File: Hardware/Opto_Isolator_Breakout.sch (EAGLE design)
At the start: 16 parts, among them Q1 NPN, Q2 NPN, U1 OPTO

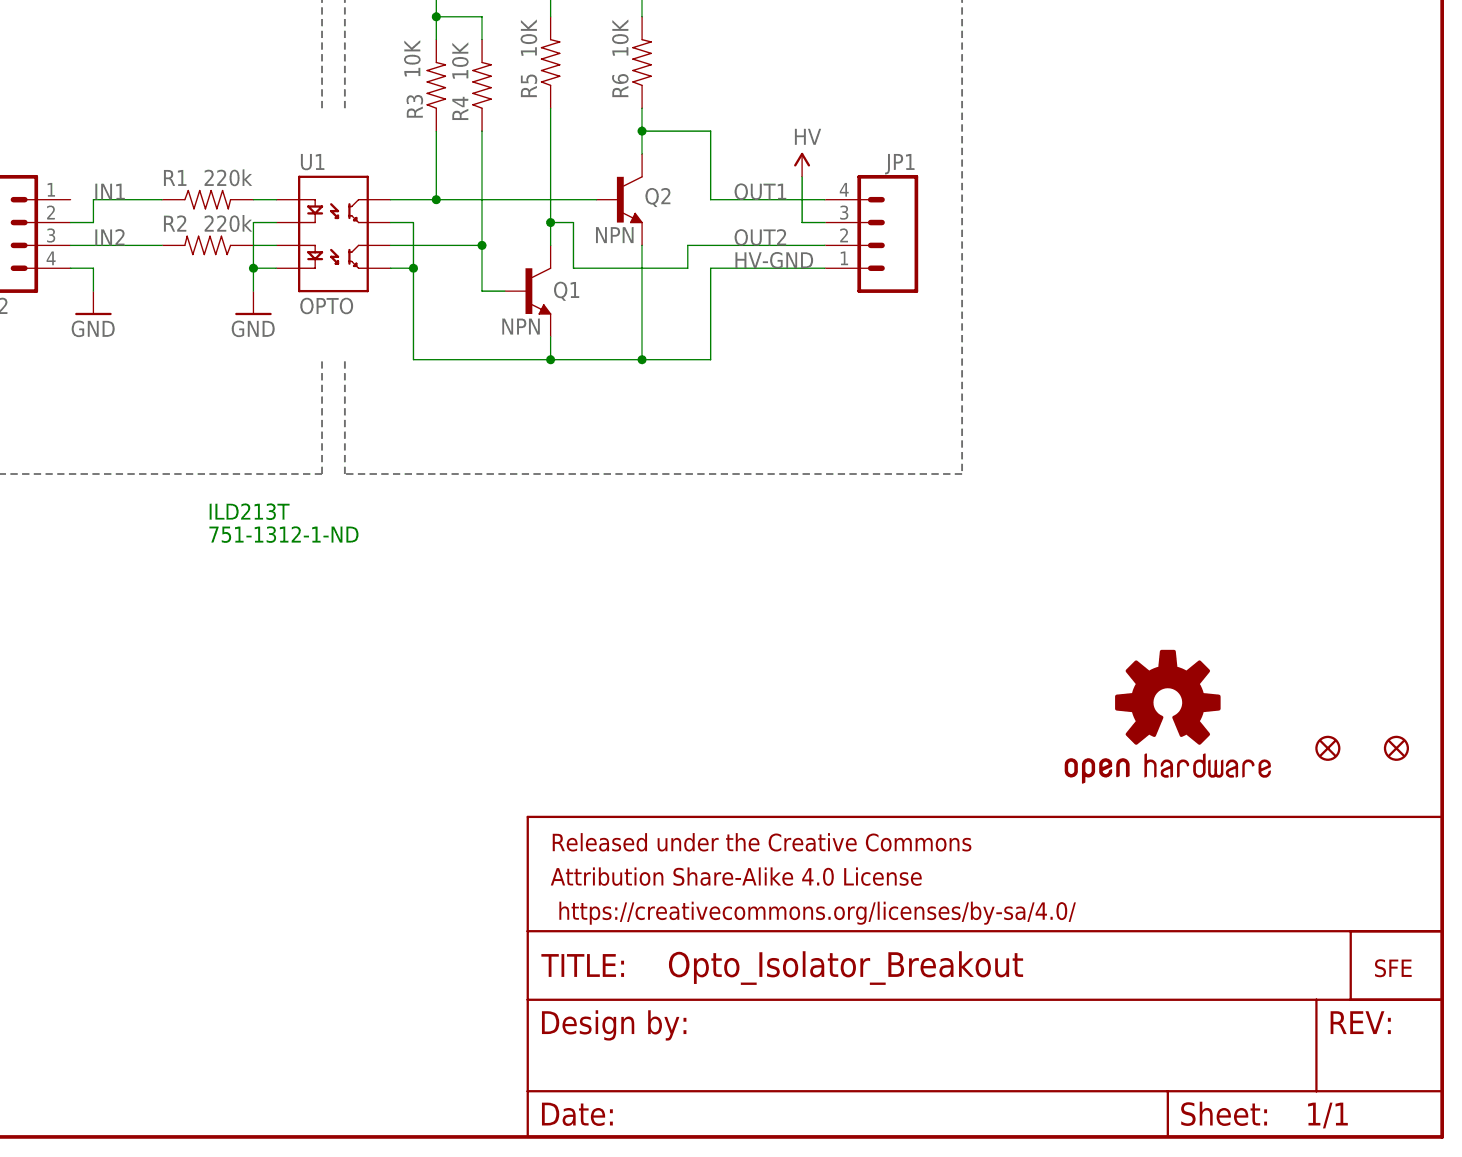
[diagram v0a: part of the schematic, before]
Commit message: Changed Res Values / SCH cleanup
changed r1 and r2 to 200K

Added version # and eng to board/sch files
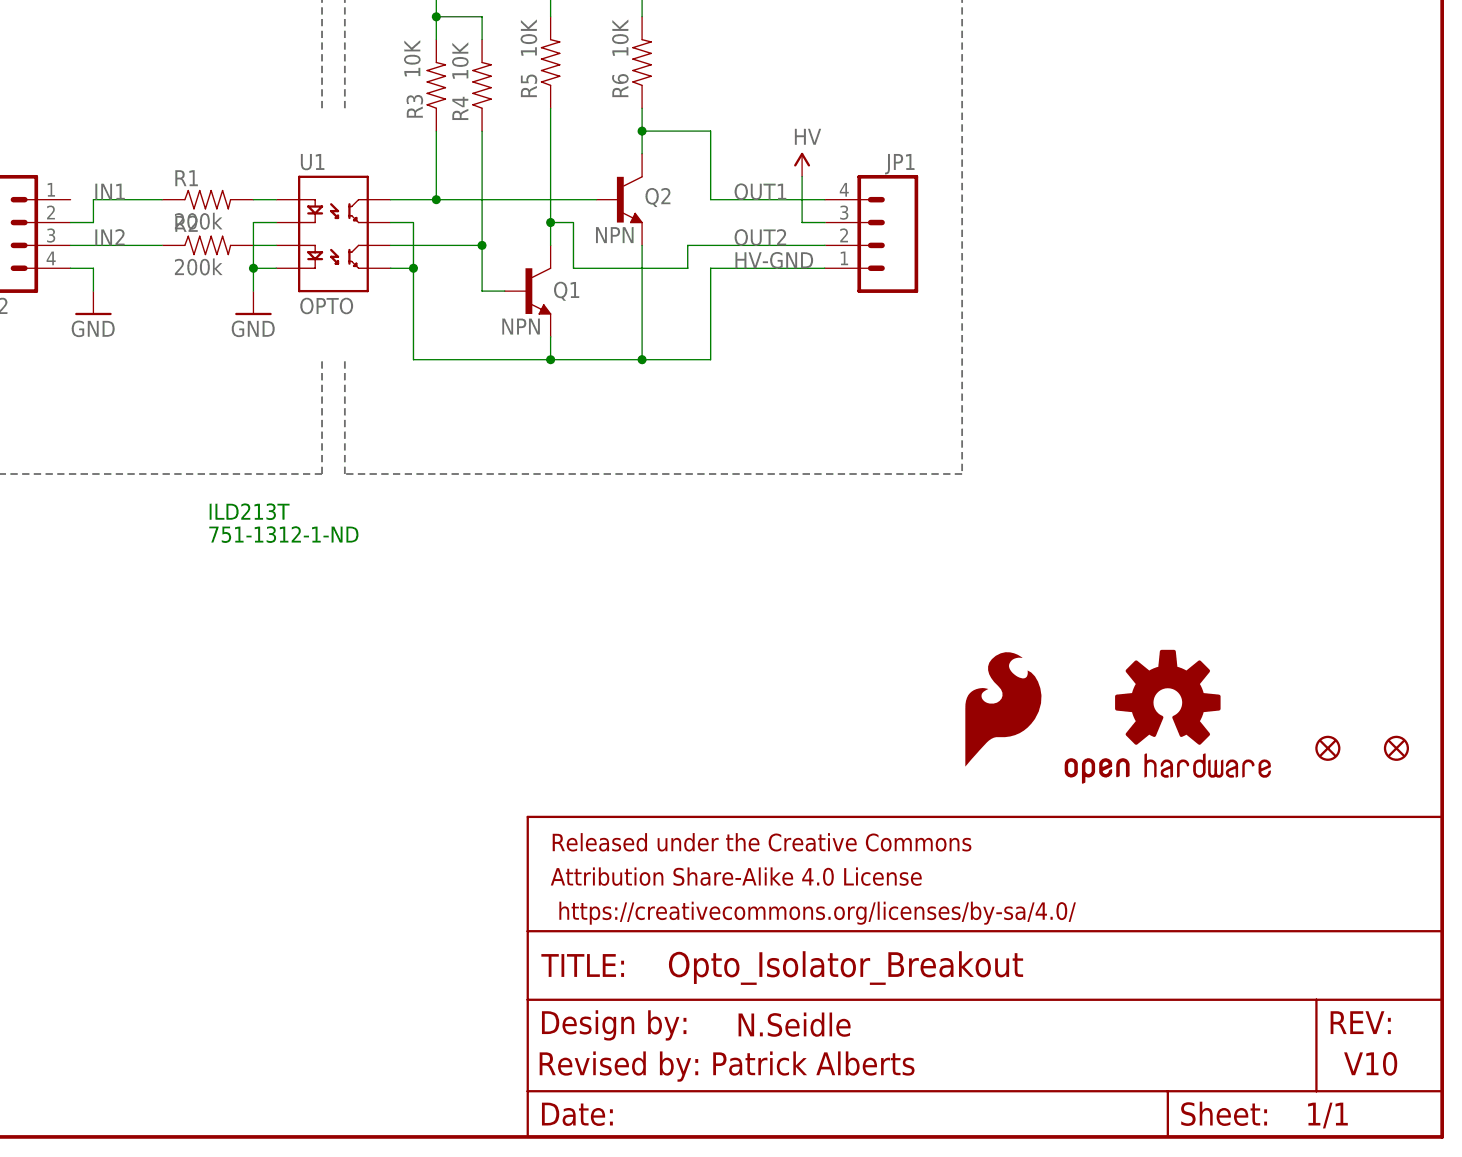
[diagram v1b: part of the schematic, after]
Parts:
- removed U$1: LOGO-SFESK, SparkFun:LOGO-SFESK
- added LOGO2: SFE_LOGO_FLAME.1_INCH, SparkFun-Aesthetics:SFE_LOGO_FLAME.1_INCH
- R1, R2: value 220k -> 200k; device SparkFun-Resistors:220KOHM1/10W1%(0603) -> SparkFun-Resistors:200KOHM1/10W1%(0603)200K
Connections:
- net IN2: now also R2.1; no longer R2.2
- net N$2: now also R2.2; no longer R2.1
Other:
- note added: "N.Seidle"
- note added: "Revised by: Patrick Alberts"
- note added: "V10"
- moved on the sheet: R2
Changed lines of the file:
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@@
 <?xml version="1.0" encoding="utf-8"?>
 <!DOCTYPE eagle SYSTEM "eagle.dtd">
-<eagle version="7.1.0">
+<eagle version="6.4">
 <drawing>
 <settings>
@@
 <part name="FRAME1" library="SparkFun-Aesthetics" deviceset="FRAME-LETTER" device=""/>
 <part name="U1" library="SparkFun" deviceset="OPTOISOLATOR-2" device="SOIC8" value="OPTO"/>
-<part name="R1" library="SparkFun-Resistors" deviceset="220KOHM1/10W1%(0603)" device="" value="220k"/>
 <part name="R3" library="SparkFun-Resistors" deviceset="10KOHM1/10W1%(0603)" device="0603" value="10K"/>
-<part name="R2" library="SparkFun-Resistors" deviceset="220KOHM1/10W1%(0603)" device="" value="220k"/>
 <part name="GND1" library="SparkFun" deviceset="GND" device=""/>
 <part name="P+1" library="SparkFun" deviceset="VCC" device="" value="HV"/>
 <part name="R4" library="SparkFun-Resistors" deviceset="10KOHM1/10W1%(0603)" device="0603" value="10K"/>
 <part name="P+2" library="SparkFun" deviceset="VCC" device="" value="HV"/>
-<part name="U$1" library="SparkFun" deviceset="LOGO-SFE" device="SK"/>
 <part name="GND4" library="SparkFun" deviceset="GND" device=""/>
 <part name="JP1" library="SparkFun-Connectors" deviceset="M04" device="PTH"/>
@@
 <part name="U$3" library="SparkFun-Aesthetics" deviceset="FIDUCIAL" device="UFIDUCIAL"/>
 <part name="LOGO1" library="SparkFun-Aesthetics" deviceset="OSHW-LOGO" device="S"/>
+<part name="LOGO2" library="SparkFun-Aesthetics" deviceset="SFE_LOGO_FLAME" device=".1_INCH"/>
+<part name="R1" library="SparkFun-Resistors" deviceset="200KOHM1/10W1%(0603)" device="200K" value="200k"/>
+<part name="R2" library="SparkFun-Resistors" deviceset="200KOHM1/10W1%(0603)" device="200K" value="200k"/>
 </parts>
 <sheets>
@@
 <text x="83.82" y="137.16" size="1.778" layer="95">3V to 5V System</text>
 <text x="175.26" y="137.16" size="1.778" layer="95">Noisy System</text>
+<text x="237.998" y="6.858" size="2.54" layer="94">V10</text>
+<text x="148.336" y="6.858" size="2.54" layer="94">Revised by: Patrick Alberts</text>
+<text x="170.434" y="11.176" size="2.54" layer="94">N.Seidle</text>
 </plain>
 <instances>
@@
 <instance part="FRAME1" gate="G$2" x="147.32" y="0"/>
 <instance part="U1" gate="G$1" x="127" y="99.06"/>
-<instance part="R1" gate="G$1" x="111.76" y="104.14" smashed="yes">
-<attribute name="NAME" x="106.68" y="105.664" size="1.778" layer="95"/>
-<attribute name="VALUE" x="111.252" y="105.664" size="1.778" layer="96"/>
-</instance>
 <instance part="R3" gate="G$1" x="137.16" y="116.84" smashed="yes" rot="R90">
 <attribute name="NAME" x="135.6614" y="113.03" size="1.778" layer="95" rot="R90"/>
 <attribute name="VALUE" x="135.382" y="117.602" size="1.778" layer="96" rot="R90"/>
-</instance>
-<instance part="R2" gate="G$1" x="111.76" y="99.06" smashed="yes" rot="R180">
-<attribute name="NAME" x="106.68" y="100.584" size="1.778" layer="95"/>
-<attribute name="VALUE" x="111.252" y="100.584" size="1.778" layer="96"/>
 </instance>
 <instance part="GND1" gate="1" x="116.84" y="91.44"/>
@@
 </instance>
 <instance part="P+2" gate="1" x="177.8" y="106.68"/>
-<instance part="U$1" gate="G$1" x="241.3" y="17.78"/>
 <instance part="GND4" gate="1" x="99.06" y="91.44"/>
 <instance part="JP1" gate="G$1" x="185.42" y="99.06" rot="MR0"/>
@@
 <instance part="U$3" gate="G$1" x="243.84" y="43.18"/>
 <instance part="LOGO1" gate="G$1" x="218.44" y="48.26"/>
+<instance part="LOGO2" gate="G$1" x="195.58" y="40.64"/>
+<instance part="R1" gate="G$1" x="111.76" y="104.14"/>
+<instance part="R2" gate="G$1" x="111.76" y="99.06"/>
 </instances>
 <busses>
@@
 <wire x1="116.84" y1="99.06" x2="119.38" y2="99.06" width="0.1524" layer="91"/>
 <pinref part="U1" gate="G$1" pin="A2"/>
-<pinref part="R2" gate="G$1" pin="1"/>
+<pinref part="R2" gate="G$1" pin="2"/>
 </segment>
 </net>
@@
 <label x="99.06" y="99.06" size="1.778" layer="95"/>
 <pinref part="JP2" gate="G$1" pin="3"/>
-<pinref part="R2" gate="G$1" pin="2"/>
+<pinref part="R2" gate="G$1" pin="1"/>
 </segment>
 </net>
@@
 <wire x1="99.06" y1="101.6" x2="96.52" y2="101.6" width="0.1524" layer="91"/>
 <label x="99.06" y="104.14" size="1.778" layer="95"/>
+<pinref part="JP2" gate="G$1" pin="2"/>
 <pinref part="R1" gate="G$1" pin="1"/>
-<pinref part="JP2" gate="G$1" pin="2"/>
-</segment>
-</net>
+</segment>
+</net>

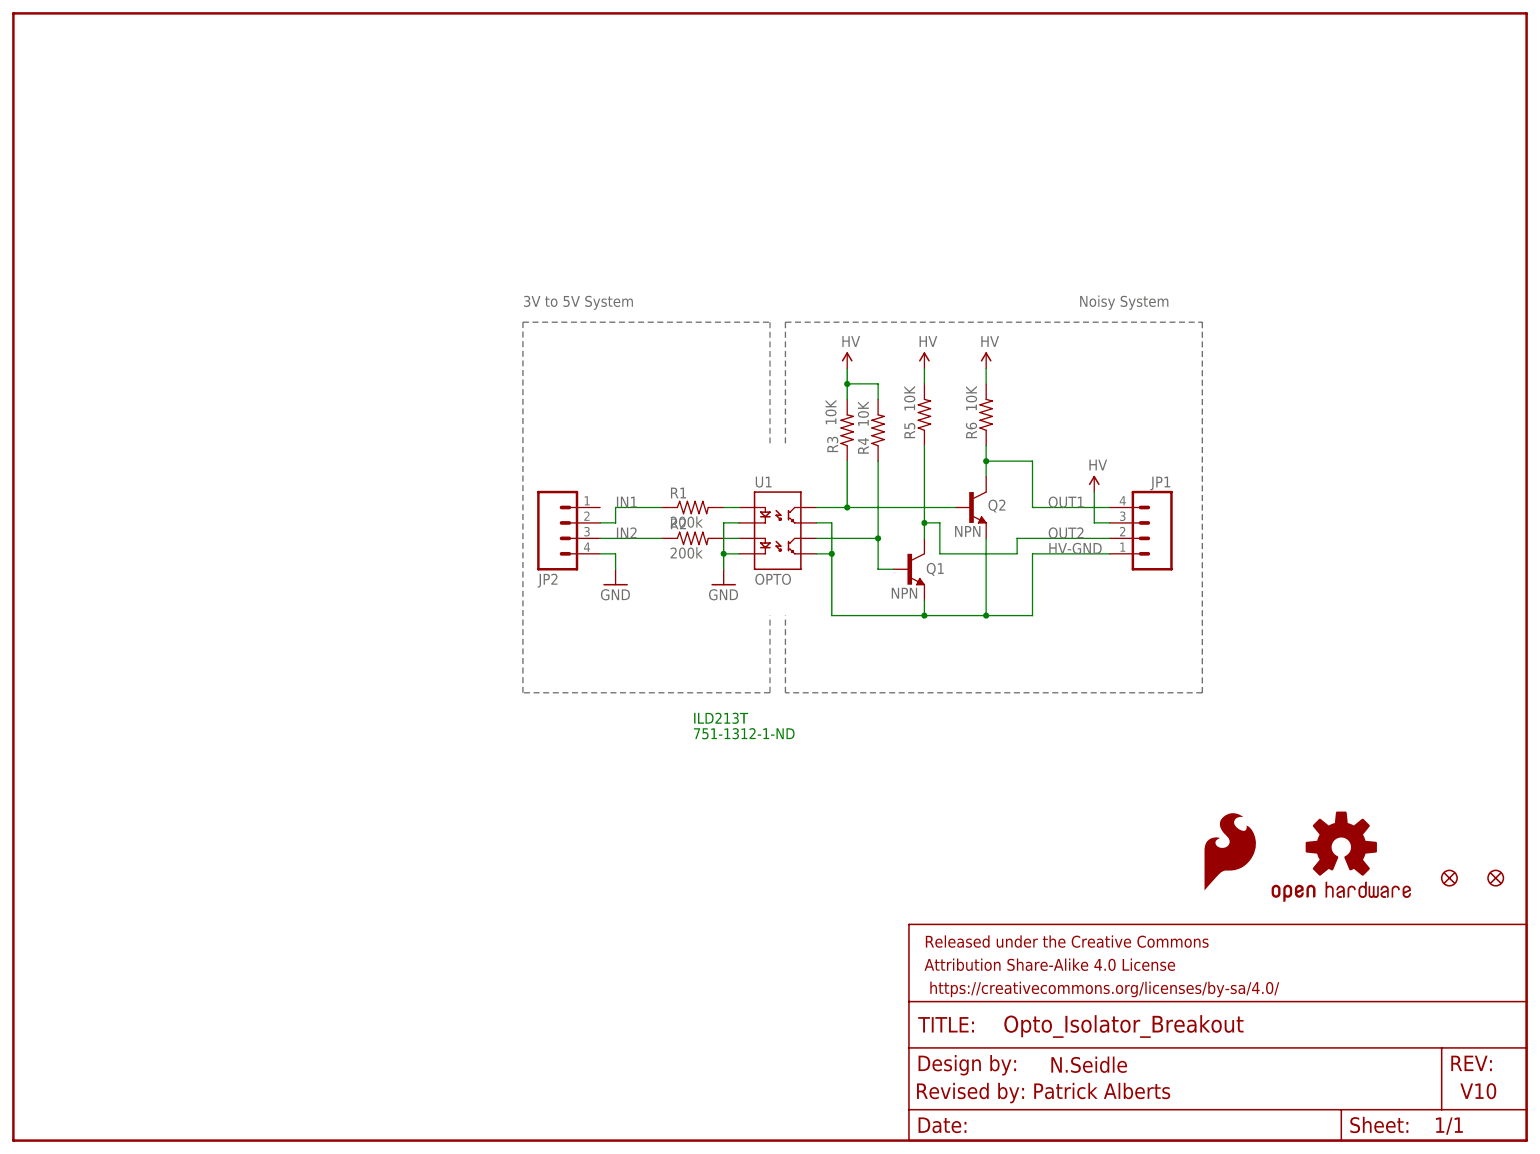
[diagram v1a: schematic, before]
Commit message: Added attributes for IC IDL213T
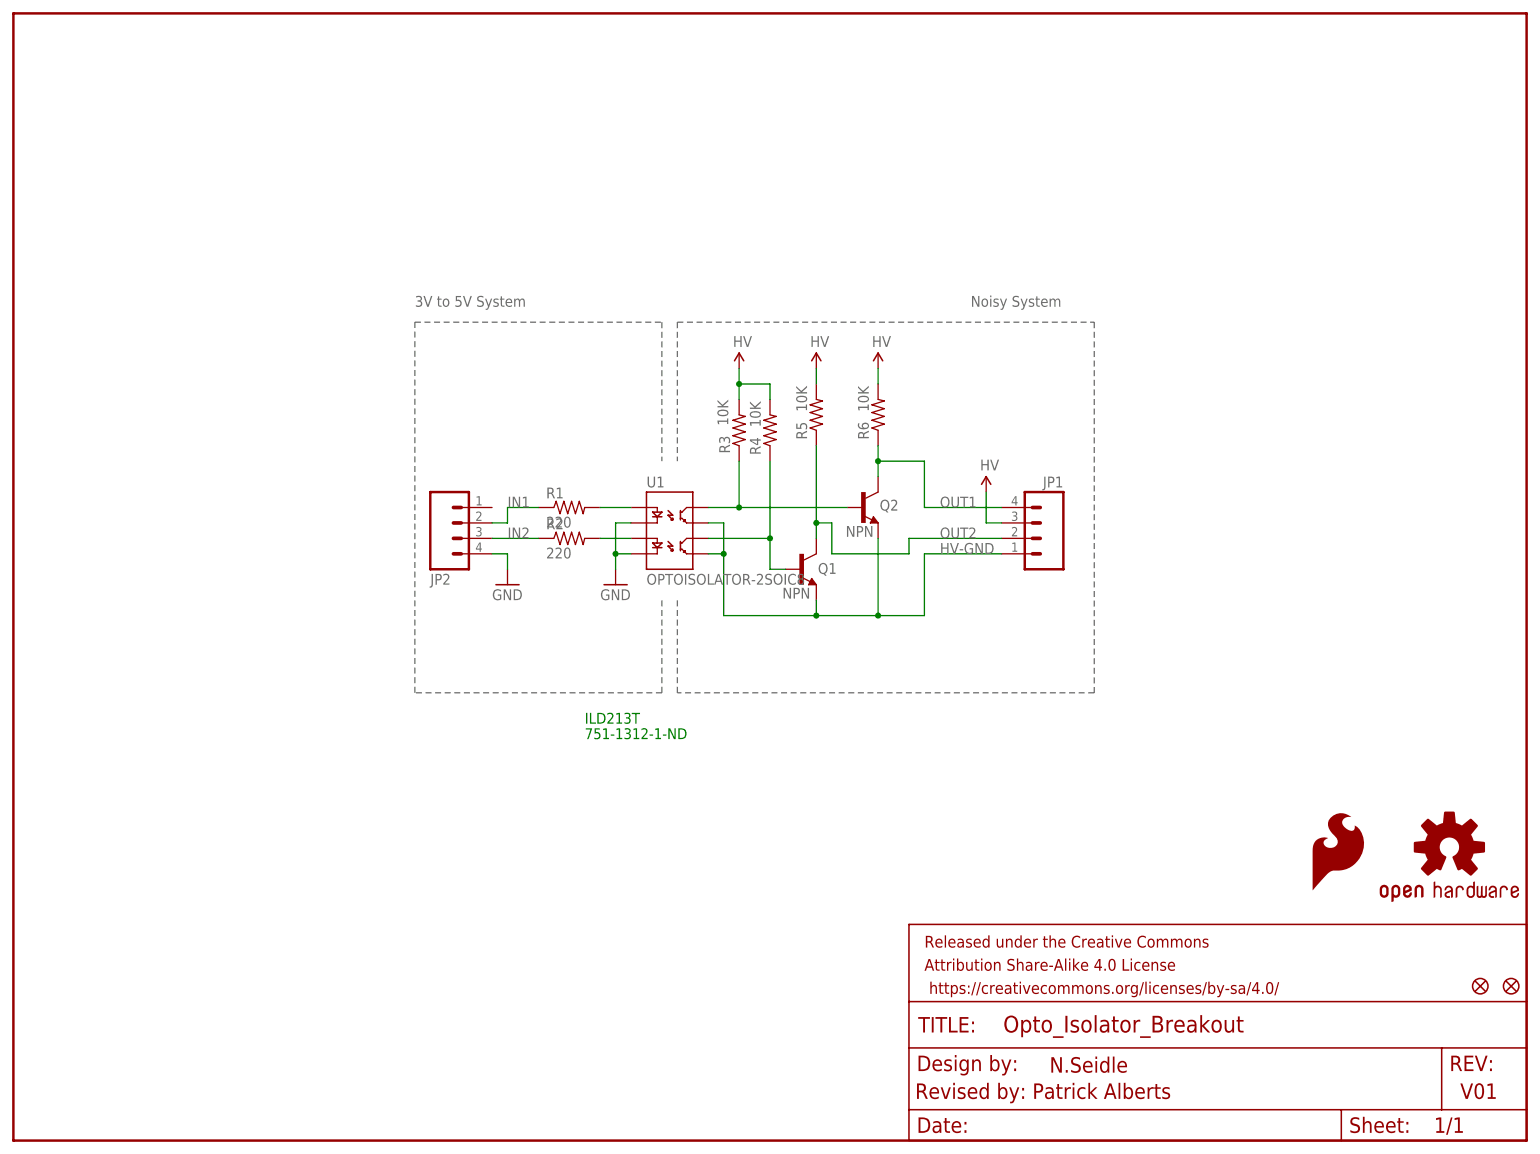
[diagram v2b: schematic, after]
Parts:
- Q1, Q2: device SparkFun:TRANSISTOR_NPNSOT23-3 -> SparkFun-DiscreteSemi:TRANSISTOR_NPNMMBT2222A
- R1, R2: value 200k -> 220; device SparkFun-Resistors:200KOHM1/10W1%(0603)200K -> SparkFun-Resistors:220OHM-1/10W-1%(0603)
- U1: value OPTO -> OPTOISOLATOR-2SOIC8; device SparkFun:OPTOISOLATOR-2SOIC8 -> SparkFun-DiscreteSemi:OPTOISOLATOR-2SOIC8
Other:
- note added: "V01"
- note removed: "V10"
- moved on the sheet: JP1, JP2, Q1, Q2, R1, R2, R3, R4, R5, R6
